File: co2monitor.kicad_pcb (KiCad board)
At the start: 2 copper layers, 55 x 58 mm, 34 parts, among them J1 USB_C_Receptacle_USB2.0, J2 UART, SW1 RESET, SW2 BOOT, U1 AP2112K-3.3, U2 ESP32-S3-WROOM-1, U3 BME680, U4 SCD40, U5 74AHCT1G125

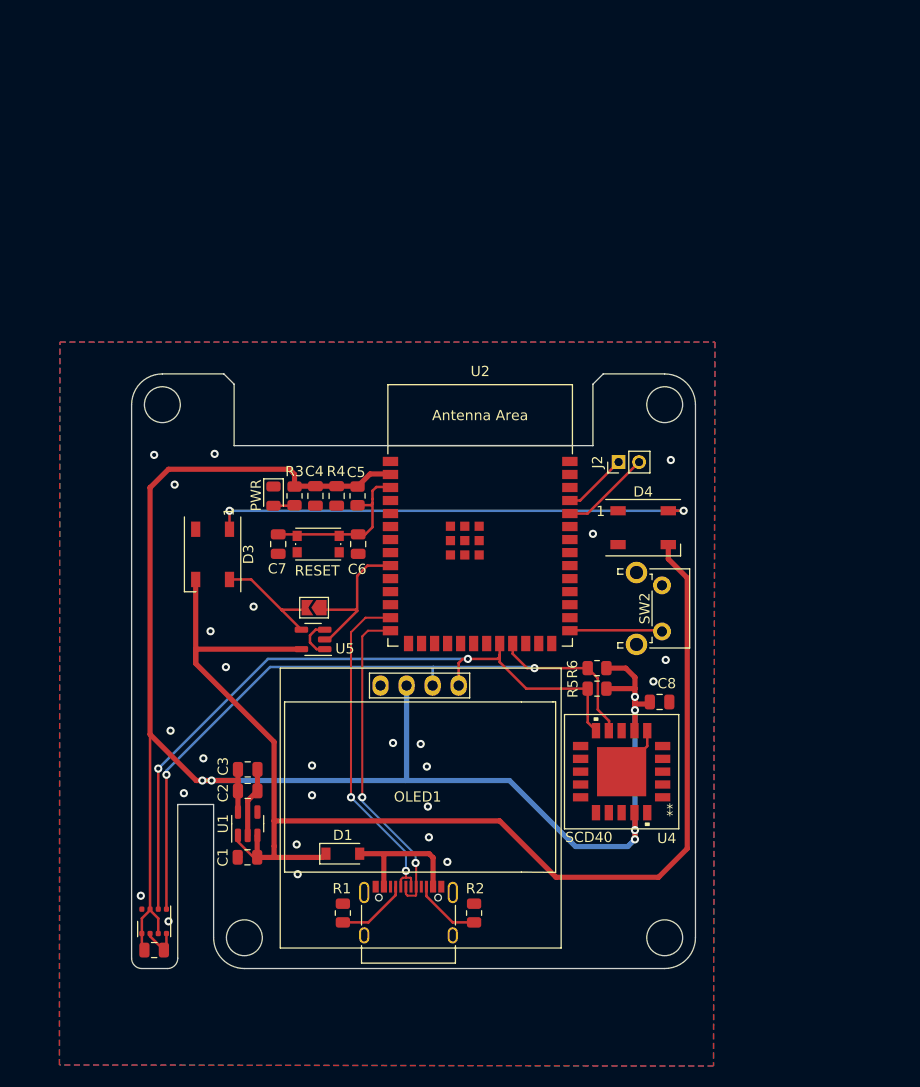
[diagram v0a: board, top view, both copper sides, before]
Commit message: Attempt #2
- Larger board (aesthetics)
- Add SHT30 for more accurate temperature measurements
- Larger tracks
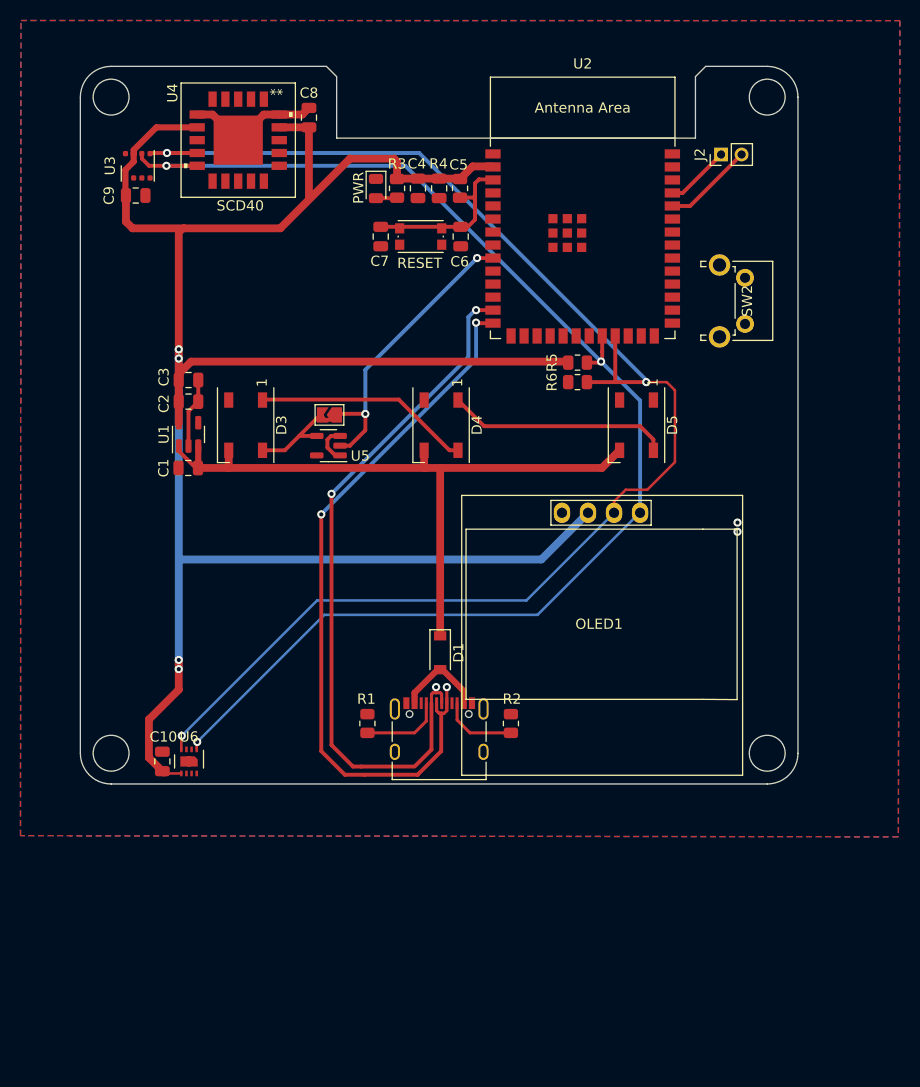
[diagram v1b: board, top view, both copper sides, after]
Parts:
- added C10: 100nF, Capacitor_SMD:C_0805_2012Metric, F.Cu at (108.0, 137.8)
- added D5: NeoPixel_THT, LED_SMD:LED_WS2812B_PLCC4_5.0x5.0mm_P3.2mm, F.Cu at (154.2, 105.0)
- added U6: SHT30-DIS, Local:SHT30_DFN-8-1EP_2.5x2.5mm_P0.5mm_EP1.1x1.7mm, F.Cu at (110.6, 137.8)
- moved U3 73.7 mm to (105.6, 79.7)
- moved C9 73.6 mm to (105.4, 82.6)
- moved U4 72.1 mm to (115.4, 77.2), turned to -90 degrees
- moved C8 66.5 mm to (122.3, 75.0), turned to -90 degrees
- moved C1 38.4 mm to (110.5, 109.2)
- moved C3 38.4 mm to (110.5, 100.6)
- moved U1 38.4 mm to (110.5, 105.9)
- moved C2 38.4 mm to (110.5, 102.7)
- moved R5 31.9 mm to (148.5, 98.9), turned to 180 degrees
- moved C4 31.6 mm to (132.9, 81.9)
- moved C5 31.6 mm to (135.0, 81.9)
- moved C6 31.6 mm to (137.1, 86.6)
- moved C7 31.6 mm to (129.3, 86.6)
- moved D2 31.6 mm to (128.8, 81.9)
- moved H2 31.6 mm to (167.0, 73.0)
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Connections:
- D4 pad 1: unconnected-(D4-Pad1) -> Net-(D4-Pad1)
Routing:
- net /SCL: track 71.2 -> 142.2 mm, vias 2 -> 3
- net +5V: track 127.2 -> 67.2 mm
- net /SDA: track 70.9 -> 130.0 mm, vias 2 -> 5
- net /D+: track 32.4 -> 71.8 mm, vias 2 -> 3
- net +3V3: track 173.8 -> 211.5 mm, vias 6 -> 4
- net /D-: track 33.2 -> 69.2 mm, vias 2 -> 3
- net Net-(D3-Pad1): track 47.6 -> 21.1 mm, vias 2 -> 0
- net Net-(D4-Pad1): track 0.00 -> 21.7 mm
- net /NPXL: track 14.9 -> 28.7 mm, vias 0 -> 2
- net /BOOT: track 9.05 -> 0.00 mm
- net GND: track 20.2 -> 24.7 mm, vias 25 -> 0
- net Net-(D1-Pad2): track 13.3 -> 9.67 mm
- net Net-(D3-Pad4): track 11.5 -> 8.94 mm
- net Net-(J1-PadA5): track 7.08 -> 7.97 mm
- net Net-(J1-PadB5): track 6.63 -> 7.41 mm
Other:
- board size 55 x 58 mm -> 70 x 70 mm

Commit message: Add logo
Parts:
- moved SW2 0.60 mm to (164.8, 91.2)
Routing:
- net GND: track 24.7 -> 36.9 mm, vias 0 -> 33
- net /BOOT: track 0.00 -> 7.37 mm
- net +3V3: track 211.5 -> 215.3 mm
- net /D+: track 71.8 -> 69.8 mm, vias 3 -> 2
- net +5V: track 67.2 -> 68.2 mm
- net /D-: track 69.2 -> 68.6 mm, vias 3 -> 2
- net /SDA: vias 5 -> 3
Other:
- board text added: "Ventilation Monitor"

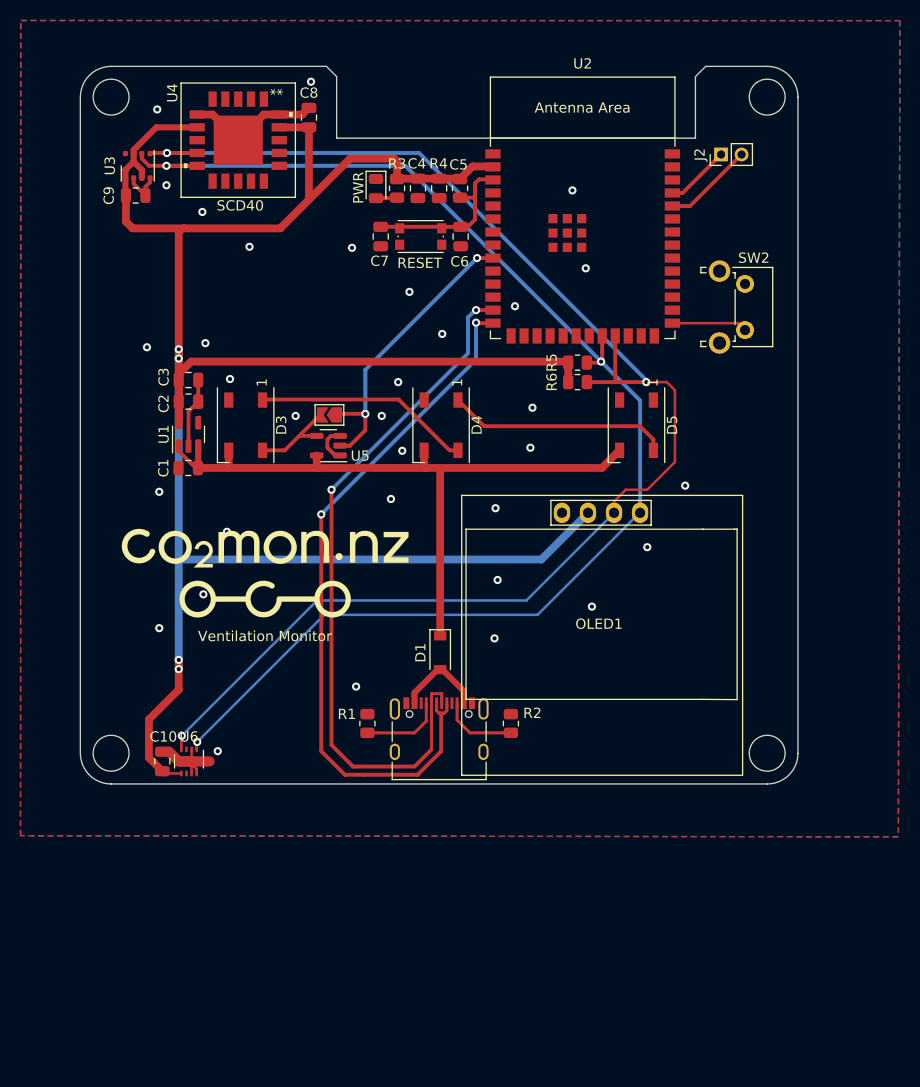
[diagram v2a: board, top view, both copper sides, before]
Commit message: Fix neopixel pinout/footprint
Turns out the NEOPIXEL_THT and WS2812B symbols have differing pinouts,
the WS2812B one appears to match reality, which required a slight
re-layout once the associated footprint changed.

Also fixed/enlarged a few ground tracks in the power-supply noticed
while inspecting the new area fills.

Credit to oseiler2 for spotting the pinout issue.
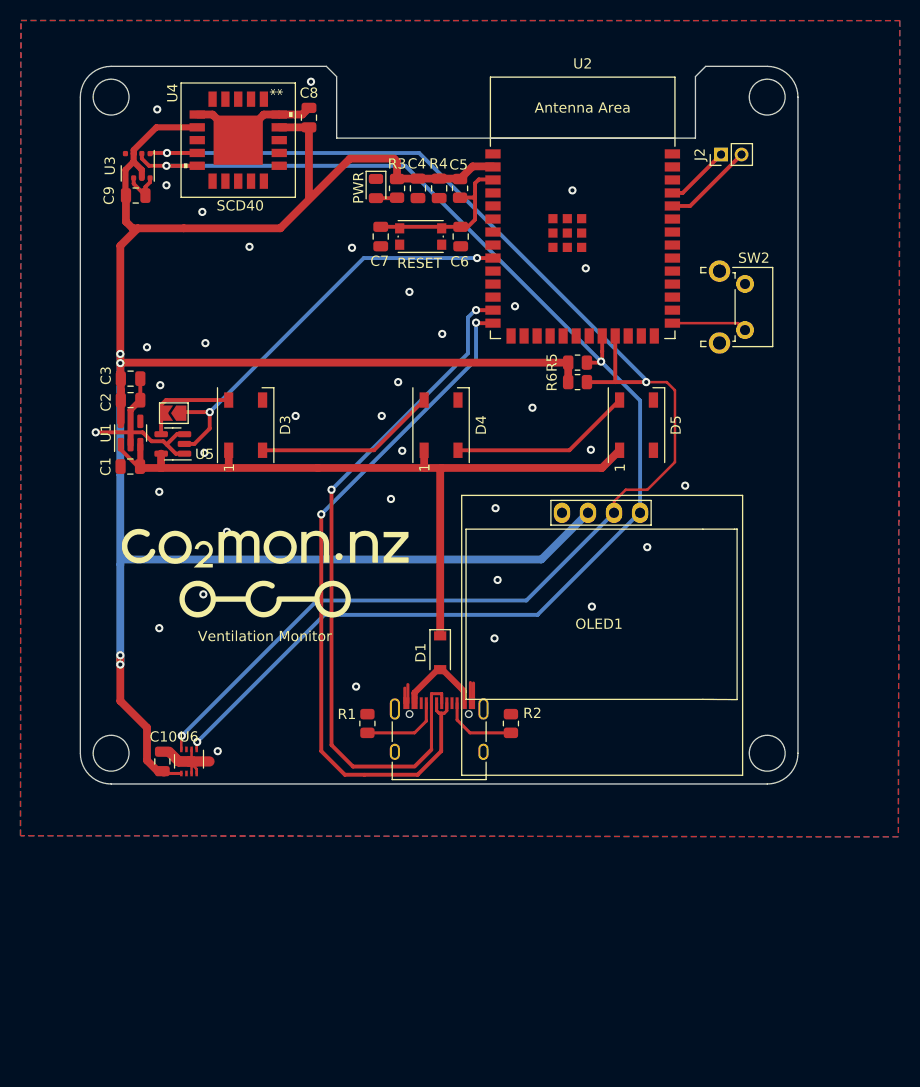
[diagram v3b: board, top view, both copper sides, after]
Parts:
- moved U5 15.2 mm to (109.0, 106.8)
- moved JP1 15.2 mm to (109.1, 103.8)
- moved C1 5.65 mm to (104.9, 109.0)
- moved C2 5.65 mm to (104.9, 102.6)
- moved C3 5.65 mm to (104.9, 100.5)
- moved U1 5.65 mm to (104.9, 105.8)
- turned D3 to 90 degrees
- turned D4 to 90 degrees
- turned D5 to 90 degrees
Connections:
- D3 pad 1: Net-(D3-Pad1) -> +5V
- D3 pad 2: GND -> Net-(D3-Pad2)
- D3 pad 3: +5V -> GND
- D4 pad 1: Net-(D4-Pad1) -> +5V
- D4 pad 2: GND -> Net-(D4-Pad2)
- D4 pad 3: +5V -> GND
- D4 pad 4: Net-(D3-Pad1) -> Net-(D3-Pad2)
- D5 pad 1: unconnected-(D5-Pad1) -> +5V
- D5 pad 2: GND -> unconnected-(D5-Pad2)
- D5 pad 3: +5V -> GND
- D5 pad 4: Net-(D4-Pad1) -> Net-(D4-Pad2)
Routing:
- net Net-(D4-Pad1): track 21.7 -> 0.00 mm
- net Net-(D3-Pad1): track 21.1 -> 0.00 mm
- net Net-(D4-Pad2): track 0.00 -> 17.8 mm
- net Net-(D3-Pad2): track 0.00 -> 17.8 mm
- net GND: track 36.9 -> 52.8 mm, vias 33 -> 35
- net /NPXL: track 28.7 -> 41.3 mm
- net +3V3: track 215.3 -> 226.5 mm
- net +5V: track 68.2 -> 74.1 mm
- net Net-(D3-Pad4): track 8.94 -> 9.82 mm

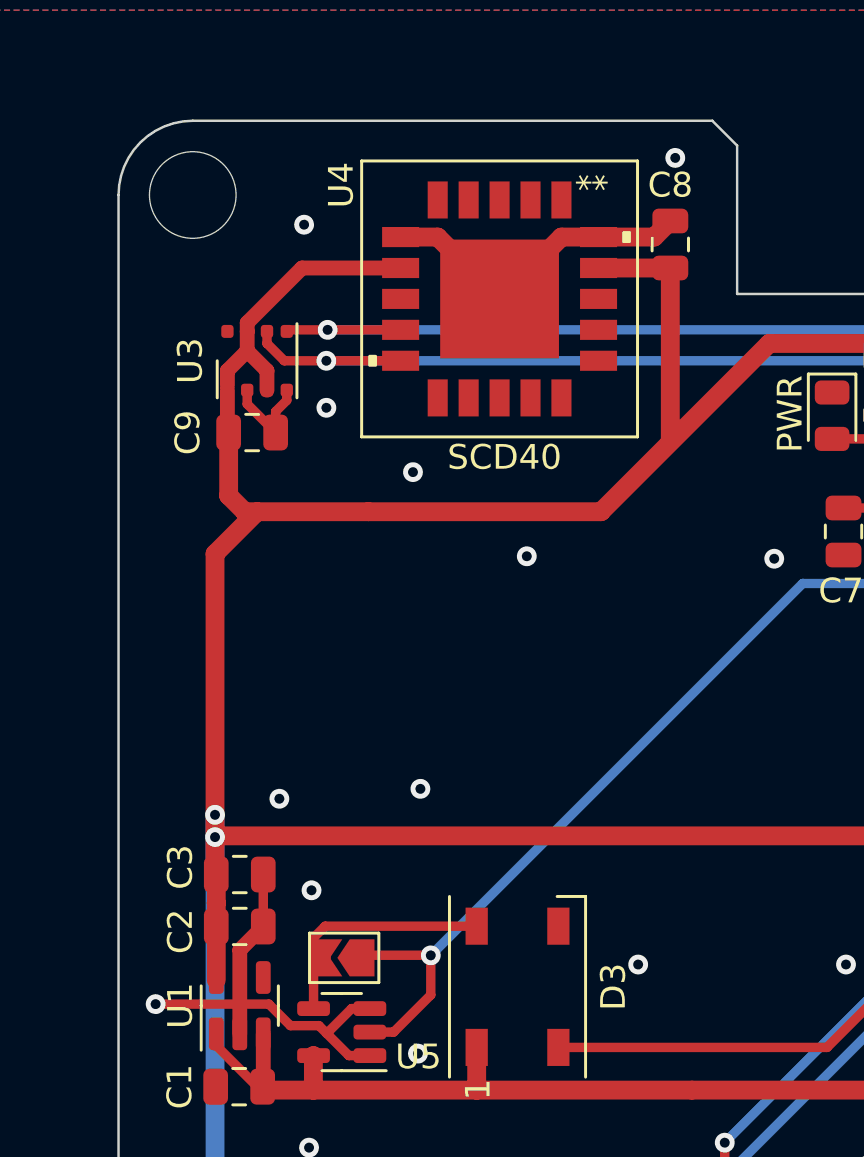
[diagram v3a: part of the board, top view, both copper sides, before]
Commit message: Tweak a few more ground tracks
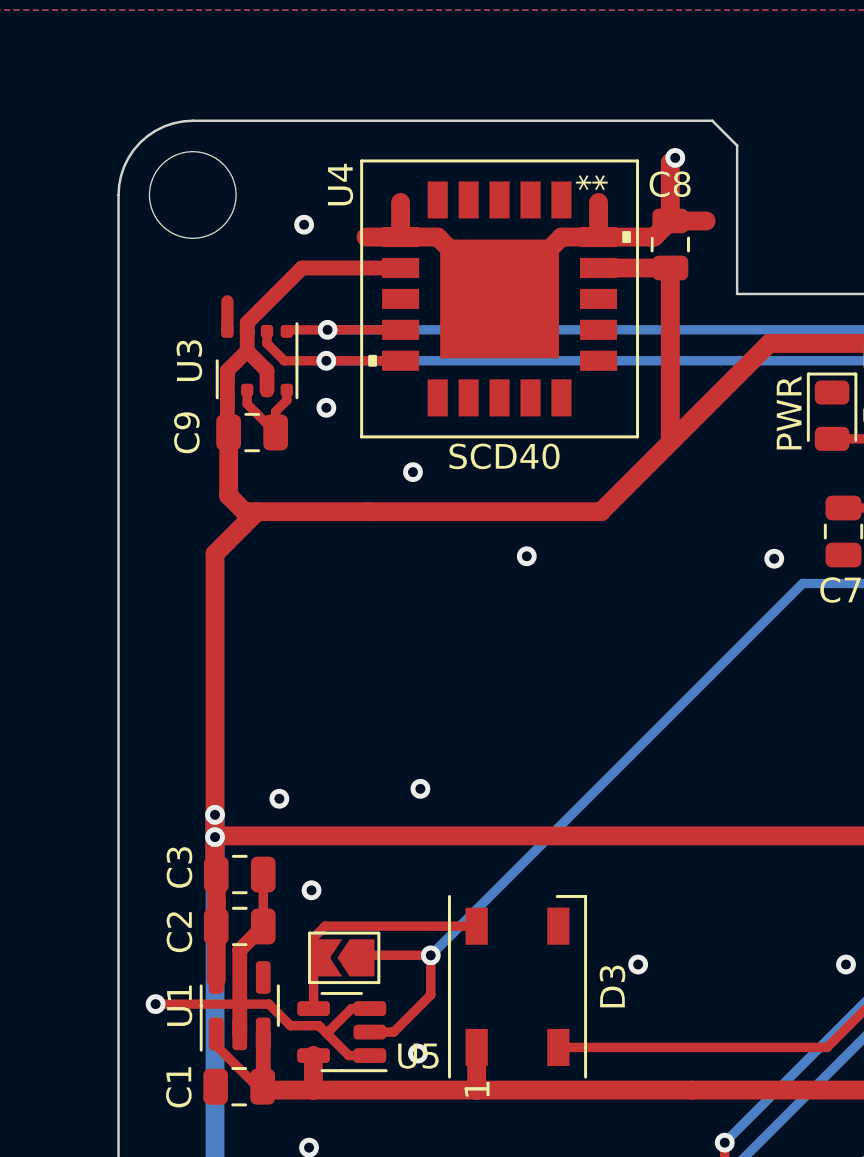
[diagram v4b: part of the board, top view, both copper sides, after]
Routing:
- net GND: track 52.8 -> 62.2 mm
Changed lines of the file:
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@@
   (segment (start 105.2 81.45) (end 106.35 82.6) (width 0.381) (layer "F.Cu") (net 1))
   (segment (start 104.9 105.7) (end 101.5 105.7) (width 0.381) (layer "F.Cu") (net 1))
+  (segment (start 122.3 74.05) (end 122.3 71.7) (width 0.762) (layer "F.Cu") (net 1))
   (segment (start 110.157191 107.780309) (end 109.309073 107.780309) (width 0.381) (layer "F.Cu") (net 1))
   (segment (start 106.35 81.75) (end 106.35 82.6) (width 0.381) (layer "F.Cu") (net 1))
@@
   (segment (start 110.85 136.625) (end 110.85 137.55) (width 0.254) (layer "F.Cu") (net 1))
   (segment (start 119.4 74.7) (end 117.9 74.7) (width 0.762) (layer "F.Cu") (net 1))
+  (segment (start 104.4 78.5125) (end 104.4 77.3) (width 0.5) (layer "F.Cu") (net 1))
   (segment (start 106.947691 106.570809) (end 106.076882 105.7) (width 0.381) (layer "F.Cu") (net 1))
   (segment (start 109.419691 105.880309) (end 108.414382 106.885618) (width 0.381) (layer "F.Cu") (net 1))
   (segment (start 138.35 132.1175) (end 138.35 130.15) (width 0.301) (layer "F.Cu") (net 1))
+  (segment (start 122.3 71.7) (end 122.5 71.5) (width 0.762) (layer "F.Cu") (net 1))
   (segment (start 106.076882 105.7) (end 104.9 105.7) (width 0.381) (layer "F.Cu") (net 1))
+  (segment (start 119.4 74.7) (end 119.4 73.3) (width 0.762) (layer "F.Cu") (net 1))
   (segment (start 108.65 136.85) (end 109.6 137.8) (width 1) (layer "F.Cu") (net 1))
   (segment (start 109.6 137.8) (end 110.6 137.8) (width 1) (layer "F.Cu") (net 1))
   (segment (start 105.2 80.8875) (end 105.2 81.45) (width 0.381) (layer "F.Cu") (net 1))
+  (segment (start 111.4 74.7) (end 111.4 73.3) (width 0.762) (layer "F.Cu") (net 1))
   (segment (start 131.95 132.1175) (end 131.95 130.3) (width 0.3) (layer "F.Cu") (net 1))
   (segment (start 110.85 138.975) (end 110.85 138.05) (width 0.254) (layer "F.Cu") (net 1))
@@
   (segment (start 119.4 74.7) (end 121.65 74.7) (width 0.762) (layer "F.Cu") (net 1))
   (segment (start 138.05 132.1175) (end 138.05 130.1) (width 0.3) (layer "F.Cu") (net 1))
+  (segment (start 122.3 74.05) (end 123.75 74.05) (width 0.762) (layer "F.Cu") (net 1))
   (segment (start 131.65 132.1175) (end 131.65 130.65) (width 0.31) (layer "F.Cu") (net 1))
   (segment (start 106.8 80.8875) (end 106.8 81.3) (width 0.381) (layer "F.Cu") (net 1))
-  (segment (start 101.5 105.7) (end 101.4 105.7) (width 0.381) (layer "F.Cu") (net 1))
+  (segment (start 111.4 74.7) (end 110 74.7) (width 0.762) (layer "F.Cu") (net 1))
   (segment (start 110.85 138.05) (end 110.6 137.8) (width 0.254) (layer "F.Cu") (net 1))
   (segment (start 111.4 74.7) (end 112.9 74.7) (width 0.762) (layer "F.Cu") (net 1))
@@
   (via (at 129.4 104.1) (size 0.8) (drill 0.4) (layers "F.Cu" "B.Cu") (free) (net 1))
   (via (at 107.7 111.5) (size 0.8) (drill 0.4) (layers "F.Cu" "B.Cu") (free) (net 1))
-  (via (at 101.5 105.7) (size 0.8) (drill 0.4) (layers "F.Cu" "B.Cu") (net 1))
   (via (at 149.8 107.4) (size 0.8) (drill 0.4) (layers "F.Cu" "B.Cu") (free) (net 1))
   (via (at 140.4 125.8) (size 0.8) (drill 0.4) (layers "F.Cu" "B.Cu") (free) (net 1))
@@
   (via (at 116.5 87.6) (size 0.8) (drill 0.4) (layers "F.Cu" "B.Cu") (free) (net 1))
   (via (at 122.5 71.5) (size 0.8) (drill 0.4) (layers "F.Cu" "B.Cu") (free) (net 1))
+  (via (at 101.5 105.7) (size 0.8) (drill 0.4) (layers "F.Cu" "B.Cu") (net 1))
   (via (at 142.4 93.4) (size 0.8) (drill 0.4) (layers "F.Cu" "B.Cu") (free) (net 1))
   (via (at 132.1 92) (size 0.8) (drill 0.4) (layers "F.Cu" "B.Cu") (free) (net 1))
